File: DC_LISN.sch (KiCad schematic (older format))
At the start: 53 parts, among them M1 MountingHole, M2 MountingHole, M3 MountingHole, M4 MountingHole, X1 PCB.SMAFRA.HT, X2 B8B-EH-A, X3 B8B-EH-A, X4 575-4, X5 575-4, X6 575-4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

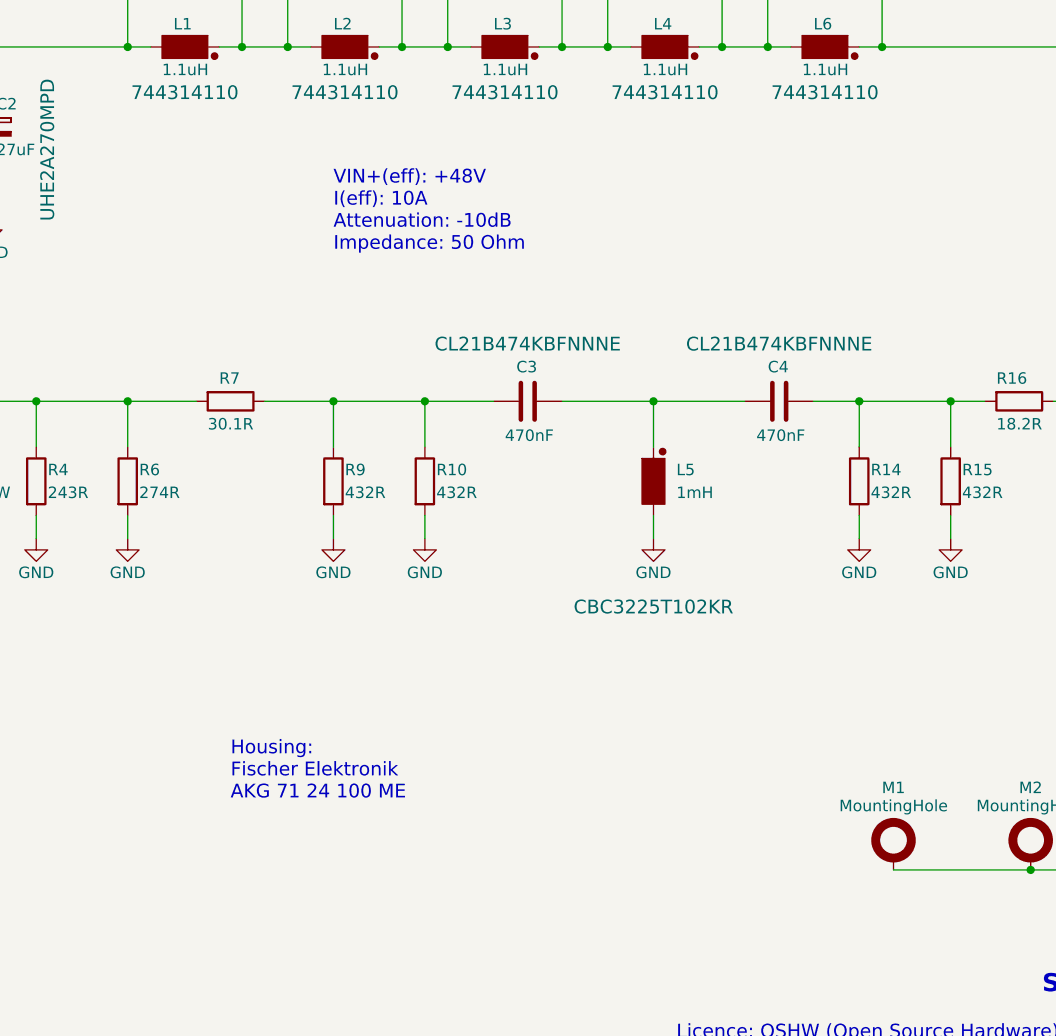
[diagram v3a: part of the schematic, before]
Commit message: Schematic: Comments updated Added binding post order numbers to comments.
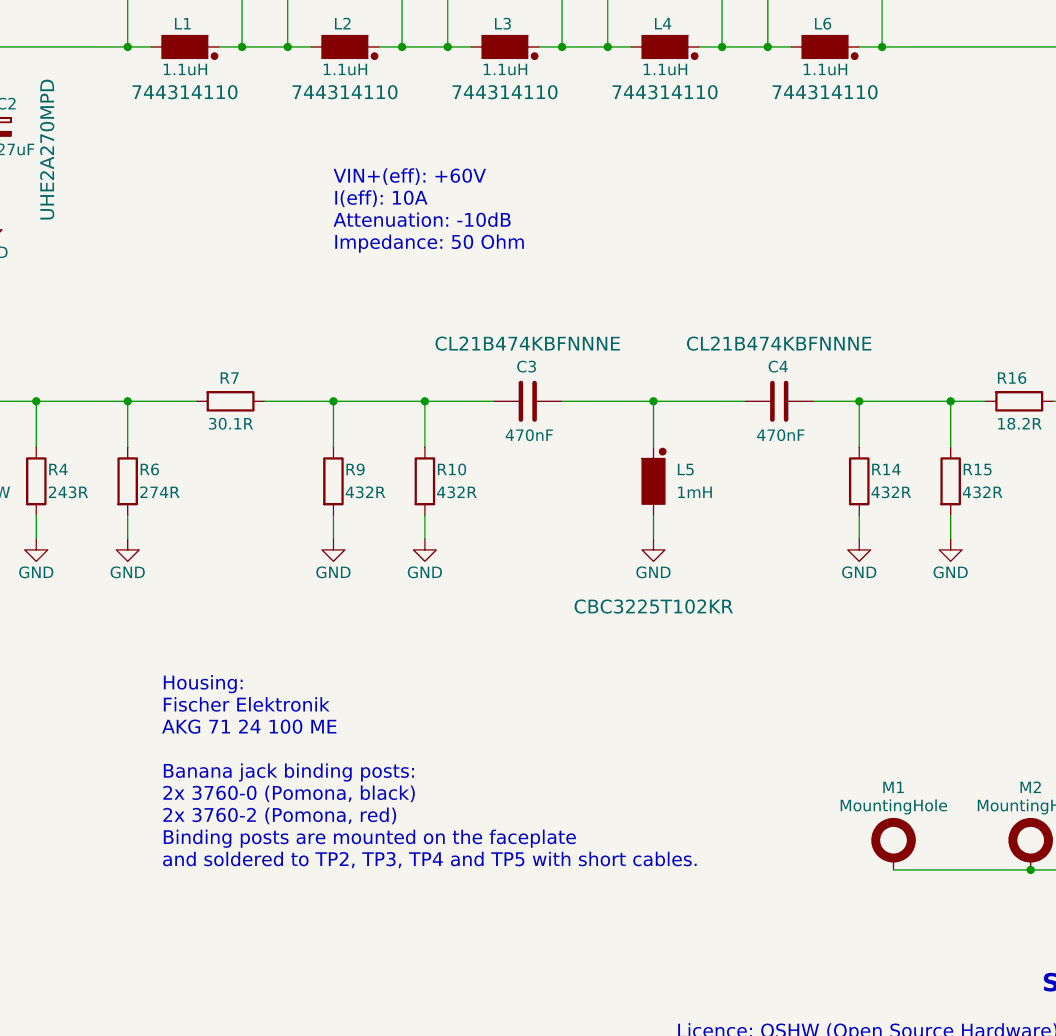
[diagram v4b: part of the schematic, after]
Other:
- note added: "Housing:\nFischer Elektronik\nAKG 71 24 100 ME\n\nBanana jack binding posts:\n2x 3760-0 (Pomona, black)\n2x 3760-2 (Pomona, red)\nBinding posts are mounted on the faceplate\nand soldered to TP2, TP3, TP4 and TP5 with short cables."
- note added: "VIN+(eff): +60V\nI(eff): 10A\nAttenuation: -10dB\nImpedance: 50 Ohm"
- note removed: "Housing:\nFischer Elektronik\nAKG 71 24 100 ME"
- note removed: "VIN+(eff): +48V\nI(eff): 10A\nAttenuation: -10dB\nImpedance: 50 Ohm"
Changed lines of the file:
@@
 This is a 5µH DC LISN intended for EMC pre compliance measurements\nof conducted emission.\nIt has an attenuation of -10dB and overvoltage protection.\nIt must be connected to a 50 Ohm spectrum anaylzer input,\nor terminated with 50 Ohm termination resistor.\nThe circuit is a partial implementation of LinearTechnology's\nDC2130A.
 Text Notes 5550 3450 0    60   ~ 0
-VIN+(eff): +48V\nI(eff): 10A\nAttenuation: -10dB\nImpedance: 50 Ohm
+VIN+(eff): +60V\nI(eff): 10A\nAttenuation: -10dB\nImpedance: 50 Ohm
 Text Notes 8200 7650 0    60   ~ 0
 19.11.2017
@@
 	8900 6150 8900 6200
 Connection ~ 2450 4100
-Text Notes 5100 5850 0    60   ~ 0
-Housing:\nFischer Elektronik\nAKG 71 24 100 ME
+Text Notes 4800 6150 0    60   ~ 0
+Housing:\nFischer Elektronik\nAKG 71 24 100 ME\n\nBanana jack binding posts:\n2x 3760-0 (Pomona, black)\n2x 3760-2 (Pomona, red)\nBinding posts are mounted on the faceplate\nand soldered to TP2, TP3, TP4 and TP5 with short cables.
 Text Notes 8650 6700 0    79   ~ 16
 SCAR001
@@
 Data
 89 50 4E 47 0D 0A 1A 0A 00 00 00 0D 49 48 44 52 00 00 00 BE 00 00 00 C8 08 03 00 00 00 61 D1 AB
-73 00 00 00 03 73 42 49 54 08 08 08 DB E1 4F E0 00 00 00 1B 50 4C 54 45 02 00 00 00 99 B0 00 99
-B1 00 9A B1 00 98 AF 00 9A B0 00 98 B0 00 99 AF 00 9A AF AE 59 D3 29 00 00 00 01 74 52 4E 53 00
+73 00 00 00 03 73 42 49 54 08 08 08 DB E1 4F E0 00 00 00 1B 50 4C 54 45 01 00 00 00 99 B0 00 99
+B1 00 9A B1 00 98 AF 00 9A B0 00 98 B0 00 99 AF 00 9A AF 1D CD FE EA 00 00 00 01 74 52 4E 53 00
 40 E6 D8 66 00 00 00 09 70 48 59 73 00 00 0F 3C 00 00 0F 3C 01 17 3A 9F 59 00 00 06 24 49 44 41
 54 78 9C ED 9D EB BA A3 2A 0C 86 05 07 F5 FE AF 78 EF 56 D1 90 04 09 4A A0 3C 8B FC 98 45 21 7C
